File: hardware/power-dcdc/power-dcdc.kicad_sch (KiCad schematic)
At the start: 83 parts, among them J1 SOLAR_IN, J2 DCDC-MEASURES, J3 DCDC-PWM, J4 BATT2, J5 BATT1, Q1 SIR186LDP, Q2 SIR186LDP, Q3 SI7149ADP, Q4 SI7149ADP, Q5 SI7149ADP, Q6 SI7149ADP, Q7 BSS123, Q8 BSS123, U1 LP4951C, U2 NCP5901B, U3 PAC1953-1, U4 DGD0215, U5 DGD0215

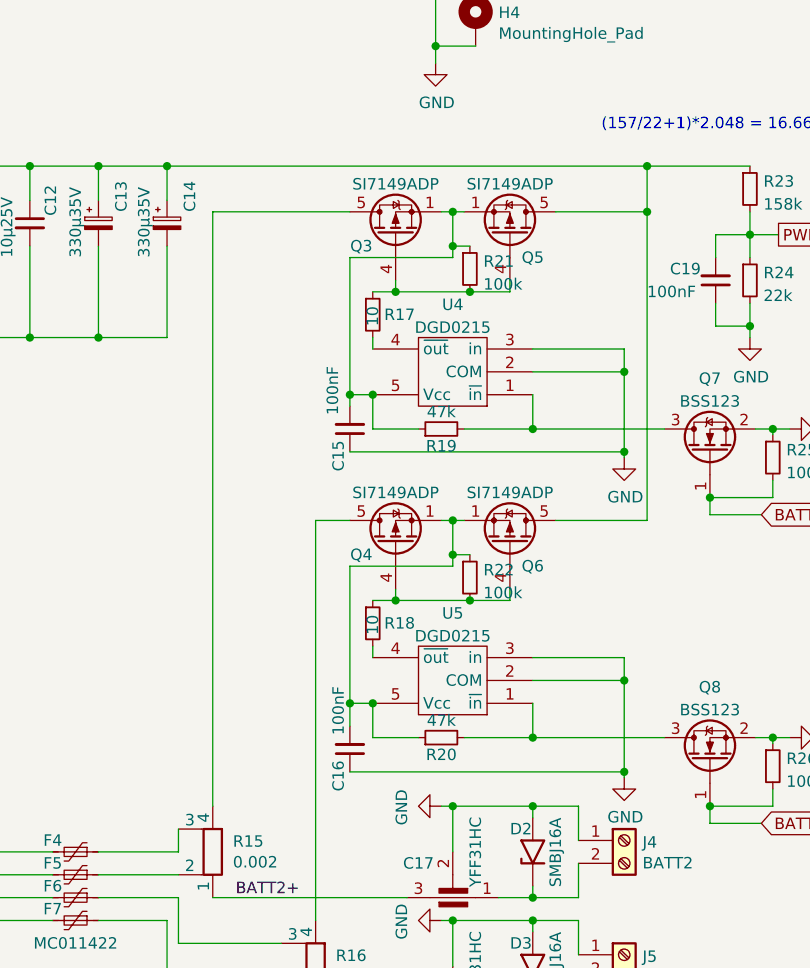
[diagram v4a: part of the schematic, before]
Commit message: Add a SMBJ16 on output of the dc/dc converter, usefull if the output mosfets are all off.
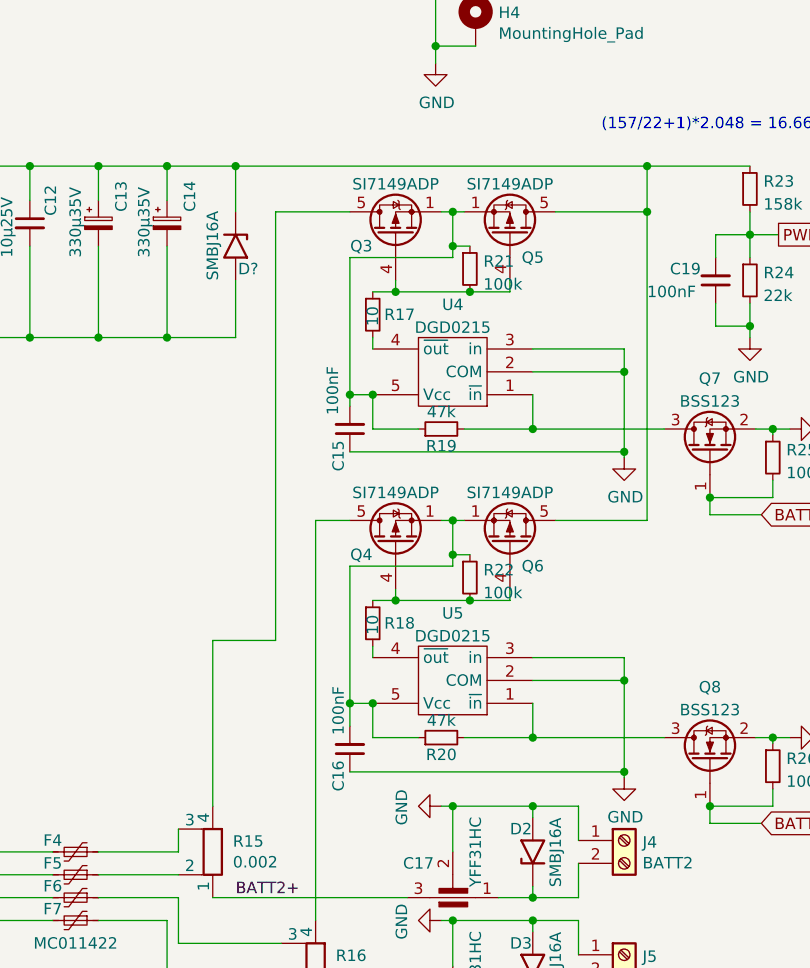
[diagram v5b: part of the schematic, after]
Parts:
- added D?: SMBJ16A, Diode_SMD:D_SMB_Handsoldering, symbol Diode:1.5KExxA
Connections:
- net GND: now also D?.2 (A2)
- net at C11.1, C12.1, C13.1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: now also D?.1 (A1)
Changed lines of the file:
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@@
   (junction (at 236.22 67.31) (diameter 0) (color 0 0 0 0)
   )
+  (junction (at 204.47 77.47) (diameter 0) (color 0 0 0 0)
+  )
   (junction (at 175.26 77.47) (diameter 0) (color 0 0 0 0)
   )
@@
   (junction (at 255.27 90.17) (diameter 0) (color 0 0 0 0)
   )
+  (junction (at 212.09 58.42) (diameter 0) (color 0 0 0 0)
+  )
   (junction (at 162.56 77.47) (diameter 0) (color 0 0 0 0)
   )
@@
     (stroke (width 0) (type default) (color 0 0 0 0))
   )
+  (wire (pts (xy 212.09 58.42) (xy 257.81 58.42))
+    (stroke (width 0) (type default) (color 0 0 0 0))
+  )
   (wire (pts (xy 196.85 139.7) (xy 205.74 139.7))
     (stroke (width 0) (type default) (color 0 0 0 0))
@@
     (stroke (width 0) (type default) (color 0 0 0 0))
   )
+  (wire (pts (xy 209.55 111.125) (xy 209.55 129.54))
+    (stroke (width 0) (type default) (color 0 0 0 0))
+  )
   (wire (pts (xy 264.795 131.445) (xy 270.51 131.445))
     (stroke (width 0) (type default) (color 0 0 0 0))
@@
     (stroke (width 0) (type default) (color 0 0 0 0))
   )
+  (wire (pts (xy 212.09 71.12) (xy 212.09 77.47))
+    (stroke (width 0) (type default) (color 0 0 0 0))
+  )
   (wire (pts (xy 110.49 129.54) (xy 110.49 121.92))
     (stroke (width 0) (type default) (color 0 0 0 0))
@@
     (stroke (width 0) (type default) (color 0 0 0 0))
   )
+  (wire (pts (xy 212.09 77.47) (xy 204.47 77.47))
+    (stroke (width 0) (type default) (color 0 0 0 0))
+  )
   (wire (pts (xy 189.23 58.42) (xy 181.61 58.42))
     (stroke (width 0) (type default) (color 0 0 0 0))
@@
     (stroke (width 0) (type default) (color 0 0 0 0))
   )
-  (wire (pts (xy 224.79 63.5) (xy 209.55 63.5))
+  (wire (pts (xy 224.79 63.5) (xy 216.535 63.5))
     (stroke (width 0) (type default) (color 0 0 0 0))
   )
@@
     (stroke (width 0) (type default) (color 0 0 0 0))
   )
+  (wire (pts (xy 212.09 58.42) (xy 212.09 63.5))
+    (stroke (width 0) (type default) (color 0 0 0 0))
+  )
   (wire (pts (xy 196.85 67.31) (xy 196.85 77.47))
     (stroke (width 0) (type default) (color 0 0 0 0))
@@
     (stroke (width 0) (type default) (color 0 0 0 0))
   )
-  (wire (pts (xy 204.47 58.42) (xy 257.81 58.42))
+  (wire (pts (xy 204.47 58.42) (xy 212.09 58.42))
     (stroke (width 0) (type default) (color 0 0 0 0))
   )
@@
     (stroke (width 0) (type default) (color 0 0 0 0))
   )
+  (wire (pts (xy 216.535 111.125) (xy 209.55 111.125))
+    (stroke (width 0) (type default) (color 0 0 0 0))
+  )
   (wire (pts (xy 83.82 147.32) (xy 95.25 147.32))
     (stroke (width 0) (type default) (color 0 0 0 0))
@@
     (stroke (width 0) (type default) (color 0 0 0 0))
   )
-  (wire (pts (xy 209.55 63.5) (xy 209.55 129.54))
+  (wire (pts (xy 216.535 63.5) (xy 216.535 111.125))
     (stroke (width 0) (type default) (color 0 0 0 0))
   )
@@
     (pin "2")
   )
+  (symbol (lib_id "Diode:1.5KExxA") (at 212.09 67.31 270) (unit 1)
+    (in_bom yes) (on_board yes)
+    (property "Reference" "D?" (id 0) (at 214.63 69.85 90)
+      (effects (font (size 1.27 1.27)) (justify right))
+    )
+    (property "Value" "SMBJ16A" (id 1) (at 209.55 71.12 0)
+      (effects (font (size 1.27 1.27)) (justify right))
+    )
+    (property "Footprint" "Diode_SMD:D_SMB_Handsoldering" (id 2) (at 207.01 67.31 0)
+      (effects (font (size 1.27 1.27)) hide)
+    )
+    (property "Datasheet" "https://www.vishay.com/docs/88301/15ke.pdf" (id 3) (at 212.09 66.04 0)
+      (effects (font (size 1.27 1.27)) hide)
+    )
+    (property "P/N" " SMBJ16Ae3/TR13 (M)" (id 4) (at 212.09 67.31 0)
+      (effects (font (size 1.27 1.27)) hide)
+    )
+    (pin "1")
+    (pin "2")
+  )
   (symbol (lib_id "Device:R_Small") (at 238.125 69.85 0) (unit 1)
     (in_bom yes) (on_board yes) (fields_autoplaced)
@@
       (reference "D3") (unit 1) (value "SMBJ16A") (footprint "Diode_SMD:D_SMB_Handsoldering")
     )
+    (path "/8c092125-0fab-431a-bae6-2fafb848292e"
+      (reference "D?") (unit 1) (value "SMBJ16A") (footprint "Diode_SMD:D_SMB_Handsoldering")
+    )
     (path "/f77ef6fe-b07a-4c34-9717-9039a3036cb9"

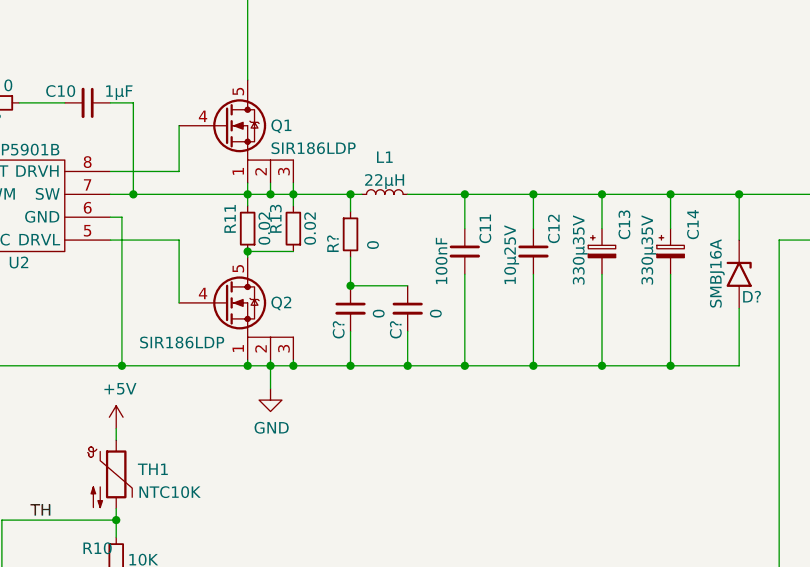
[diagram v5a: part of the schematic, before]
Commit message: Make it clear that some components are not known yet.
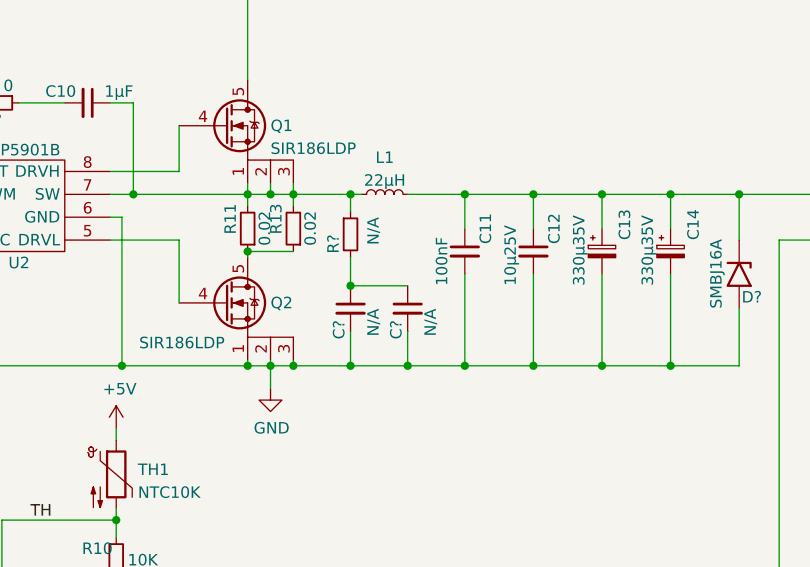
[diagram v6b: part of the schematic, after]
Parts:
- C? (x2), R?: value 0 -> N/A
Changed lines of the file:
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@@
       (effects (font (size 1.27 1.27)) (justify right))
     )
-    (property "Value" "0" (id 1) (at 172.085 71.12 90)
+    (property "Value" "N/A" (id 1) (at 171.45 71.12 90)
       (effects (font (size 1.27 1.27)) (justify right))
     )
@@
       (effects (font (size 1.27 1.27)) (justify right))
     )
-    (property "Value" "0" (id 1) (at 171.45 63.5 90)
+    (property "Value" "N/A" (id 1) (at 171.45 60.96 90)
       (effects (font (size 1.27 1.27)) (justify right))
     )
@@
       (effects (font (size 1.27 1.27)) (justify right))
     )
-    (property "Value" "0" (id 1) (at 178.435 71.12 90)
+    (property "Value" "N/A" (id 1) (at 177.8 71.12 90)
       (effects (font (size 1.27 1.27)) (justify right))
     )
@@
     )
     (path "/b3cfc9f0-a892-4f82-bbe8-f501b475d4bd"
-      (reference "C?") (unit 1) (value "0") (footprint "Capacitor_SMD:C_0805_2012Metric_Pad1.18x1.45mm_HandSolder")
+      (reference "C?") (unit 1) (value "N/A") (footprint "Capacitor_SMD:C_0805_2012Metric_Pad1.18x1.45mm_HandSolder")
     )
     (path "/e571972a-7a49-4923-8e25-84d0184724f1"
-      (reference "C?") (unit 1) (value "0") (footprint "Capacitor_SMD:C_0805_2012Metric_Pad1.18x1.45mm_HandSolder")
+      (reference "C?") (unit 1) (value "N/A") (footprint "Capacitor_SMD:C_0805_2012Metric_Pad1.18x1.45mm_HandSolder")
     )
     (path "/b97d5a53-2424-4463-9f29-8a4d0e12cc96"
@@
     )
     (path "/c86b057e-15c1-4134-8dc4-125bb3619427"
-      (reference "R?") (unit 1) (value "0") (footprint "Resistor_SMD:R_1210_3225Metric_Pad1.30x2.65mm_HandSolder")
+      (reference "R?") (unit 1) (value "N/A") (footprint "Resistor_SMD:R_1210_3225Metric_Pad1.30x2.65mm_HandSolder")
     )
     (path "/a344c995-e9f0-4656-a268-9dcc3bd6cffb"

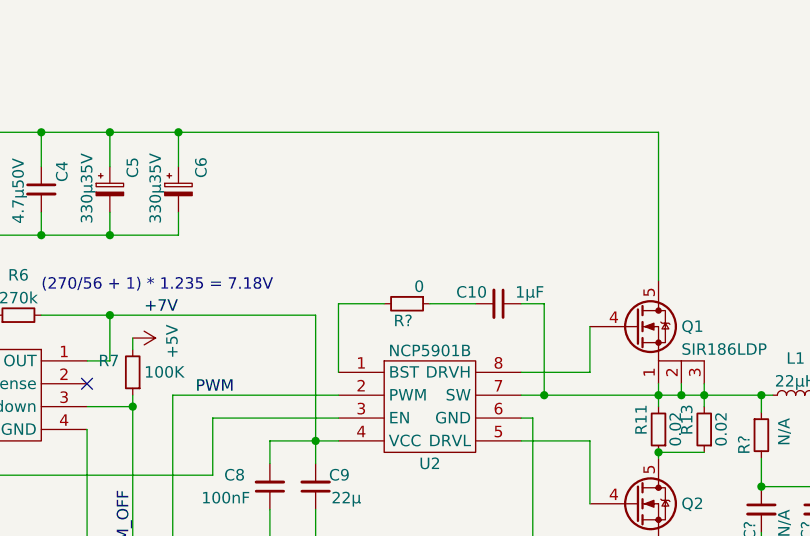
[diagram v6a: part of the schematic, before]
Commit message: Provision a schottky diode in parallel with Rboost
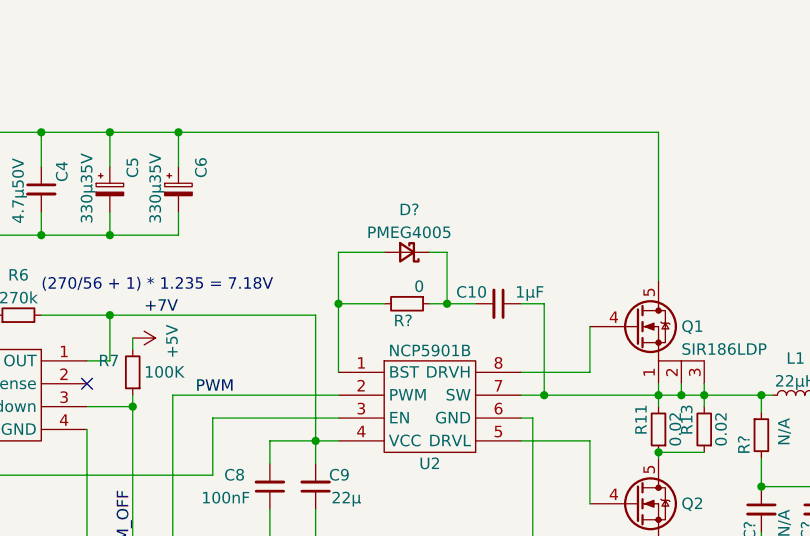
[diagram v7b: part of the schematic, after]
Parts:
- added D?: PMEG4005, Diode_SMD:D_SOD-123, symbol Device:D_Schottky_Small
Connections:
- net at R?.2, U2.1 (BST): now also D?.2 (A)
- net at C10.2, R?.1: now also D?.1 (K)
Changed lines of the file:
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@@
   (junction (at 83.82 67.31) (diameter 0) (color 0 0 0 0)
   )
+  (junction (at 121.92 48.26) (diameter 0) (color 0 0 0 0)
+  )
   (junction (at 80.01 95.25) (diameter 0) (color 0 0 0 0)
   )
@@
   (junction (at 196.85 77.47) (diameter 0) (color 0 0 0 0)
   )
+  (junction (at 133.985 48.26) (diameter 0) (color 0 0 0 0)
+  )
   (junction (at 157.48 58.42) (diameter 0) (color 0 0 0 0)
   )
@@
     (stroke (width 0) (type default) (color 0 0 0 0))
   )
-  (wire (pts (xy 132.08 48.26) (xy 137.16 48.26))
+  (wire (pts (xy 132.08 48.26) (xy 133.985 48.26))
     (stroke (width 0) (type default) (color 0 0 0 0))
   )
@@
     (stroke (width 0) (type default) (color 0 0 0 0))
   )
+  (wire (pts (xy 121.92 42.545) (xy 121.92 48.26))
+    (stroke (width 0) (type default) (color 0 0 0 0))
+  )
   (wire (pts (xy 204.47 67.31) (xy 204.47 77.47))
     (stroke (width 0) (type default) (color 0 0 0 0))
@@
     (stroke (width 0) (type default) (color 0 0 0 0))
   )
+  (wire (pts (xy 133.985 48.26) (xy 137.16 48.26))
+    (stroke (width 0) (type default) (color 0 0 0 0))
+  )
   (wire (pts (xy 108.585 128.905) (xy 108.585 132.08))
     (stroke (width 0) (type default) (color 0 0 0 0))
@@
     (stroke (width 0) (type default) (color 0 0 0 0))
   )
+  (wire (pts (xy 127 42.545) (xy 121.92 42.545))
+    (stroke (width 0) (type default) (color 0 0 0 0))
+  )
   (wire (pts (xy 224.79 102.87) (xy 224.79 118.11))
     (stroke (width 0) (type default) (color 0 0 0 0))
@@
     (stroke (width 0) (type default) (color 0 0 0 0))
   )
+  (wire (pts (xy 132.08 42.545) (xy 133.985 42.545))
+    (stroke (width 0) (type default) (color 0 0 0 0))
+  )
   (wire (pts (xy 105.41 134.62) (xy 105.41 142.24))
     (stroke (width 0) (type default) (color 0 0 0 0))
@@
     (stroke (width 0) (type default) (color 0 0 0 0))
   )
+  (wire (pts (xy 133.985 42.545) (xy 133.985 48.26))
+    (stroke (width 0) (type default) (color 0 0 0 0))
+  )
   (text "Max 28V" (at 30.48 144.78 0)
     (effects (font (size 1.27 1.27)) (justify left bottom))
@@
     (pin "1")
   )
+  (symbol (lib_id "Device:D_Schottky_Small") (at 129.54 42.545 180) (unit 1)
+    (in_bom yes) (on_board yes) (fields_autoplaced)
+    (property "Reference" "D?" (id 0) (at 129.794 37.8292 0))
+    (property "Value" "PMEG4005" (id 1) (at 129.794 40.3661 0))
+    (property "Footprint" "Diode_SMD:D_SOD-123" (id 2) (at 129.54 42.545 90)
+      (effects (font (size 1.27 1.27)) hide)
+    )
+    (property "Datasheet" "~" (id 3) (at 129.54 42.545 90)
+      (effects (font (size 1.27 1.27)) hide)
+    )
+    (pin "1")
+    (pin "2")
+  )
   (symbol (lib_id "Connector:Screw_Terminal_01x02") (at 255.27 133.35 0) (unit 1)
     (in_bom yes) (on_board yes)
@@
       (reference "D3") (unit 1) (value "SMBJ16A") (footprint "Diode_SMD:D_SMB_Handsoldering")
     )
+    (path "/2b203639-acbd-4698-a448-d60b4b99a2ea"
+      (reference "D?") (unit 1) (value "PMEG4005") (footprint "Diode_SMD:D_SOD-123")
+    )
     (path "/8c092125-0fab-431a-bae6-2fafb848292e"

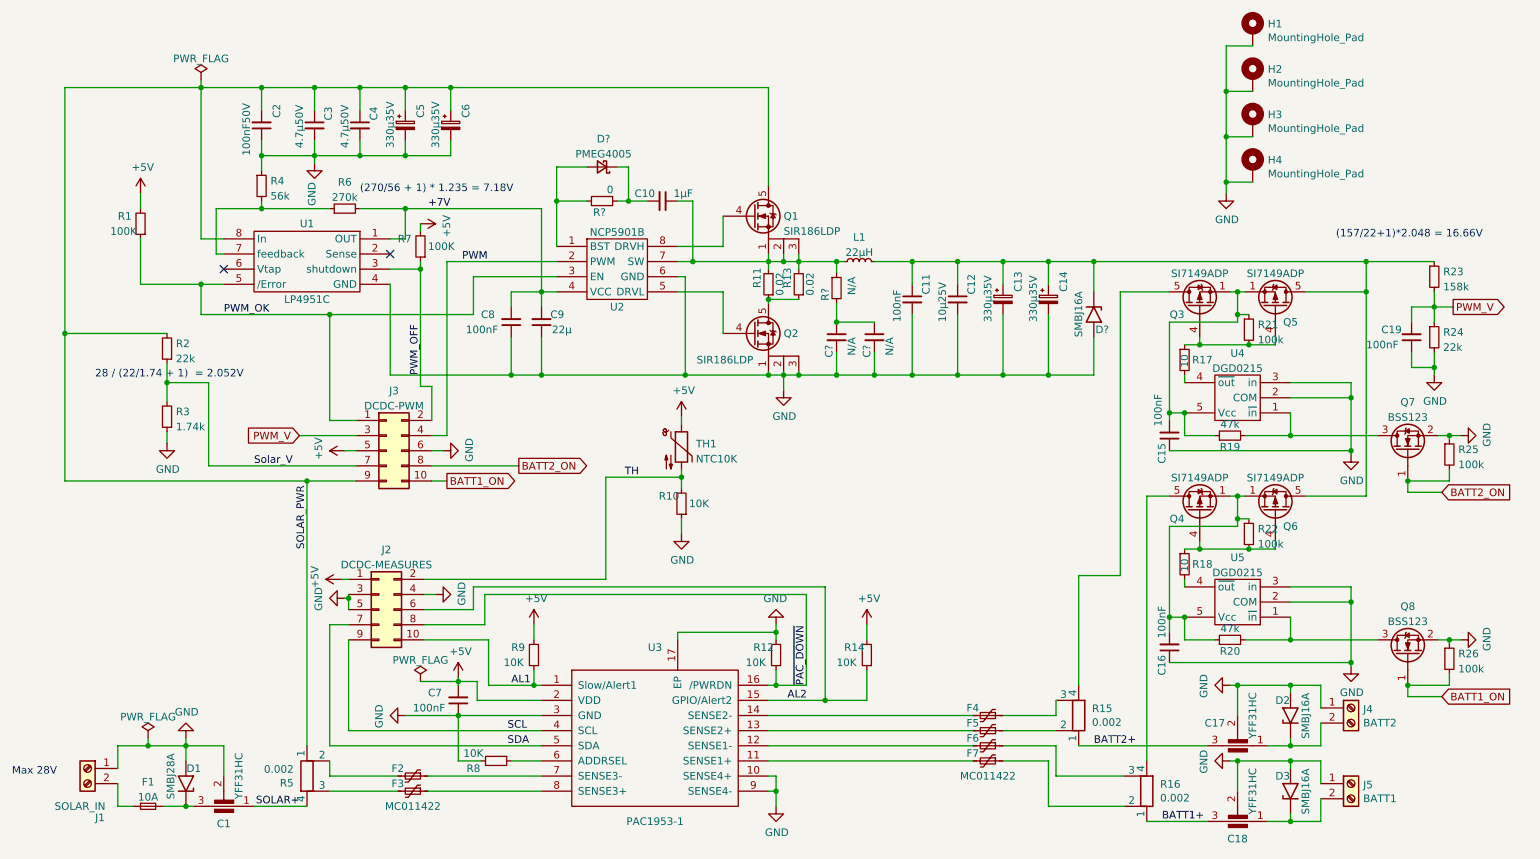
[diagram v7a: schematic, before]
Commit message: Annontate schematic again
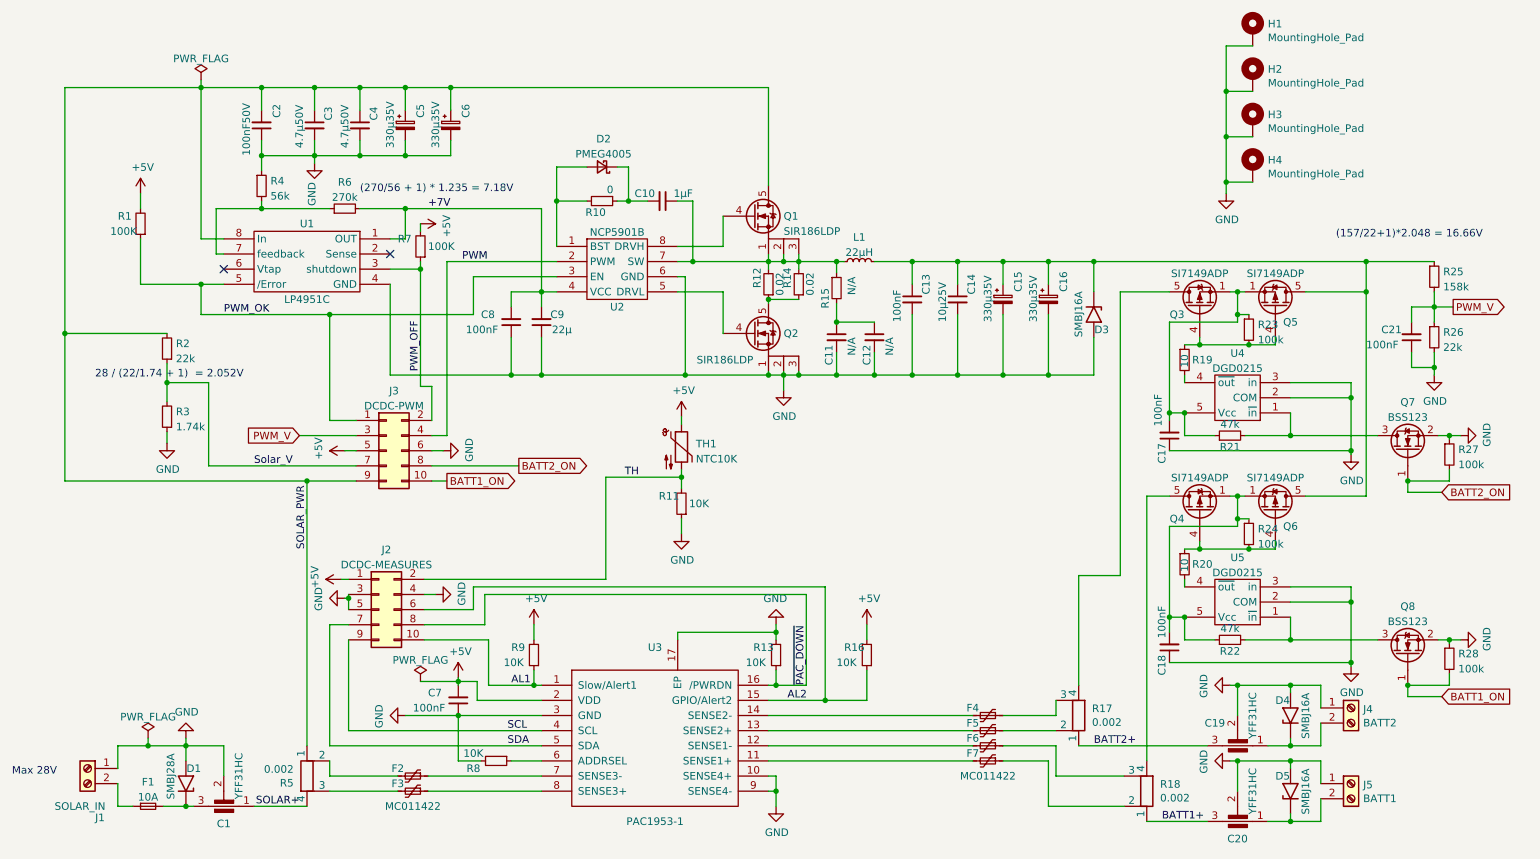
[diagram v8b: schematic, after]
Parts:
- gave numbers to parts that had none: 6
- renumbered C11 to C13, C12 to C14, C13 to C15, C14 to C16, C15 to C17, C16 to C18, C17 to C19, C18 to C20, C19 to C21, D2 to D4, D3 to D5, R10 to R11, R11 to R12, R12 to R13, R13 to R14, R14 to R16, R15 to R17, R16 to R18, R17 to R19, R18 to R20, R19 to R21, R20 to R22, R21 to R23, R22 to R24, R23 to R25, R24 to R26, R25 to R27, R26 to R28
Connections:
- net GND: no longer J3.2 (Pin_2), R7.1, U1.3 (shutdown)
- new net PWM_OFF: J3.2 (Pin_2), R7.1, U1.3 (shutdown)
